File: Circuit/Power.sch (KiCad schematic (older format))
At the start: 23 parts

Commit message: Updated Lithium power circuit
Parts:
- removed C?: 470uF 16V, symbol CP
- removed C?: 47uF 16V, symbol C
- removed C?: C, symbol C
- removed D? (x4): SS14, symbol DIODE_SCHOTTKY
- removed L?: ?uH, symbol INDUCTOR_SMALL
- removed Q?: MOSFET_P, symbol MOSFET_P
- removed Q?: MOSFET_N, symbol MOSFET_N
- removed R? (x2): 100K, symbol R
- added C?: 220uF 16V, symbol CP
- added D? (x2): SS14, symbol DIODE_SCHOTTKY
- added L?: ???uH, symbol INDUCTOR
- added Q? (x2): SS9015, symbol TRANSISTOR_PNP
- added Q?: FDN340P, symbol MOSFET_P
- added R?: 100K, symbol R
- added R? (x2): 10K, symbol R
- Q201: renamed from Q?; value MOSFET_P -> FDN340P
- Q202: renamed from Q?; value AOD4189 -> FDN340P
- R204: renamed from R?; value ? -> 8.2K
- gave numbers to parts that had none: 8
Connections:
- net labels added: GBAT, GIN, VBAT
- net labels removed: VLOAD, ~CHARGER_ON
- wire segments 66 -> 58
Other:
- note added: ""Ideal Diode OR" circuit derived from "Type 3" shown at\nhttp://www.jiggerjuice.info/electronics/projects/power/ideal-diode.html\n\nSee attached LTSpice model file."
- note added: "Charging current\nIr = 220mA max"
- note added: "Solar input:\n7V open circuit voltage panel\nNominal 4-6V under load"
- note added: "USB Input:\nPreferred charging input if available, 4.5-5.5V"
- note removed: "AOD41897 gate\nthreshold = -1.7V - -3V"
- note removed: "Extra capacitance here\nensures VBAT P-FET switches\noff instantly, but slow to switch\non (allows VIN to switch off first)\n\nValue TBD"
- note removed: "~CHARGER_ON\nLOW = <1V\nHIGH = VOUT\n\n2N7002 gate\nthreshold = 1V - 2.5V"
- moved on the sheet: BAT201, D201, LED201, LED202, Q201, Q202, R201, R202, R203, R204, U201

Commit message: Updated to use esp12e
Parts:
- gave numbers to parts that had none: 10
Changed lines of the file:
@@
 LIBS:valves
 LIBS:ESPlant
+LIBS:ESP8266
 LIBS:ESPlant-cache
 EELAYER 25 0
@@
 $EndComp
 $Comp
-L GND #PWR202
+L GND #PWR18
 U 1 1 563C4E24
 P 4000 4650
-F 0 "#PWR202" H 4000 4400 50  0001 C CNN
+F 0 "#PWR18" H 4000 4400 50  0001 C CNN
 F 1 "GND" H 4000 4500 50  0000 C CNN
 F 2 "" H 4000 4650 60  0000 C CNN
@@
 $EndComp
 $Comp
-L GND #PWR201
+L GND #PWR17
 U 1 1 563C5B2C
 P 1150 1500
-F 0 "#PWR201" H 1150 1250 50  0001 C CNN
+F 0 "#PWR17" H 1150 1250 50  0001 C CNN
 F 1 "GND" H 1150 1350 50  0000 C CNN
 F 2 "" H 1150 1500 60  0000 C CNN
@@
 Connection ~ 5200 4500
 $Comp
-L DIODE_SCHOTTKY D?
+L DIODE_SCHOTTKY D3
 U 1 1 564177C3
 P 6850 1400
-F 0 "D?" H 6850 1500 40  0000 C CNN
+F 0 "D3" H 6850 1500 40  0000 C CNN
 F 1 "SS14" H 6850 1300 40  0000 C CNN
 F 2 "" H 6850 1400 60  0000 C CNN
@@
 $EndComp
 $Comp
-L TRANSISTOR_PNP Q?
+L TRANSISTOR_PNP Q2
 U 1 1 56417A02
 P 7250 3200
-F 0 "Q?" H 7250 3350 60  0000 R CNN
+F 0 "Q2" H 7250 3350 60  0000 R CNN
 F 1 "SS9015" H 7300 3000 60  0000 R CNN
 F 2 "" H 7250 3200 60  0000 C CNN
@@
 $EndComp
 $Comp
-L TRANSISTOR_PNP Q?
+L TRANSISTOR_PNP Q4
 U 1 1 56417AB5
 P 8950 3200
-F 0 "Q?" H 8950 3350 60  0000 R CNN
+F 0 "Q4" H 8950 3350 60  0000 R CNN
 F 1 "SS9015" H 9000 3000 60  0000 R CNN
 F 2 "" H 8950 3200 60  0000 C CNN
@@
 	7450 3200 8750 3200
 $Comp
-L R R?
+L R R7
 U 1 1 56417BF7
 P 8100 3900
-F 0 "R?" V 8180 3900 50  0000 C CNN
+F 0 "R7" V 8180 3900 50  0000 C CNN
 F 1 "100K" V 8100 3900 50  0000 C CNN
 F 2 "" V 8030 3900 30  0000 C CNN
@@
 $EndComp
 $Comp
-L R R?
+L R R6
 U 1 1 56417D21
 P 7150 3900
-F 0 "R?" V 7230 3900 50  0000 C CNN
+F 0 "R6" V 7230 3900 50  0000 C CNN
 F 1 "10K" V 7150 3900 50  0000 C CNN
 F 2 "" V 7080 3900 30  0000 C CNN
@@
 $EndComp
 $Comp
-L R R?
+L R R8
 U 1 1 56417E36
 P 9050 3900
-F 0 "R?" V 9130 3900 50  0000 C CNN
+F 0 "R8" V 9130 3900 50  0000 C CNN
 F 1 "10K" V 9050 3900 50  0000 C CNN
 F 2 "" V 8980 3900 30  0000 C CNN
@@
 	7150 3400 7150 3650
 $Comp
-L GND #PWR?
+L GND #PWR19
 U 1 1 56417FB3
 P 8100 4600
-F 0 "#PWR?" H 8100 4350 50  0001 C CNN
+F 0 "#PWR19" H 8100 4350 50  0001 C CNN
 F 1 "GND" H 8100 4450 50  0000 C CNN
 F 2 "" H 8100 4600 60  0000 C CNN
@@
 Connection ~ 7150 3550
 $Comp
-L MOSFET_P Q?
+L MOSFET_P Q3
 U 1 1 5641832A
 P 8400 2600
-F 0 "Q?" V 8200 2450 60  0000 R CNN
+F 0 "Q3" V 8200 2450 60  0000 R CNN
 F 1 "FDN340P" V 8300 2450 60  0000 R CNN
 F 2 "" H 8400 2600 60  0000 C CNN
@@
 $EndComp
 $Comp
-L DIODE_SCHOTTKY D?
+L DIODE_SCHOTTKY D4
 U 1 1 56418330
 P 8400 2100
-F 0 "D?" H 8400 2200 40  0000 C CNN
+F 0 "D4" H 8400 2200 40  0000 C CNN
 F 1 "SS14" H 8400 2000 40  0000 C CNN
 F 2 "" H 8400 2100 60  0000 C CNN
@@
 Connection ~ 7100 1800
 $Comp
-L INDUCTOR L?
+L INDUCTOR L1
 U 1 1 5641A74C
 P 9500 1800
-F 0 "L?" H 9400 1900 40  0000 C CNN
+F 0 "L1" H 9400 1900 40  0000 C CNN
 F 1 "???uH" H 9500 1750 40  0000 C CNN
 F 2 "" H 9500 1800 60  0000 C CNN
@@
 $EndComp
 $Comp
-L CP C?
+L CP C3
 U 1 1 5641A7A1
 P 10250 2150
-F 0 "C?" H 10275 2250 50  0000 L CNN
+F 0 "C3" H 10275 2250 50  0000 L CNN
 F 1 "220uF 16V" H 10275 2050 50  0000 L CNN
 F 2 "" H 10288 2000 30  0000 C CNN
@@
 	10250 2300 10250 2500
 $Comp
-L GND #PWR?
+L GND #PWR20
 U 1 1 5641AA9F
 P 10250 2500
-F 0 "#PWR?" H 10250 2250 50  0001 C CNN
+F 0 "#PWR20" H 10250 2250 50  0001 C CNN
 F 1 "GND" H 10250 2350 50  0000 C CNN
 F 2 "" H 10250 2500 60  0000 C CNN

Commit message: Change battery switching circuit to use MCP6002 comparator instead
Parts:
- removed C3: 220uF 16V, symbol CP
- removed D3, D4: SS14, symbol DIODE_SCHOTTKY
- removed L1: ???uH, symbol INDUCTOR
- removed Q2, Q4: SS9015, symbol TRANSISTOR_PNP
- removed R6, R8: 10K, symbol R
- removed R7: 100K, symbol R
- added C201: 100uF 16V, symbol C
- added C?: 100nF, symbol C
- added U202: MCP6002, symbol LM193
- renumbered Q3 to Q203
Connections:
- wire segments 58 -> 48
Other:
- note removed: ""Ideal Diode OR" circuit derived from "Type 3" shown at\nhttp://www.jiggerjuice.info/electronics/projects/power/ideal-diode.html\n\nSee attached LTSpice model file."

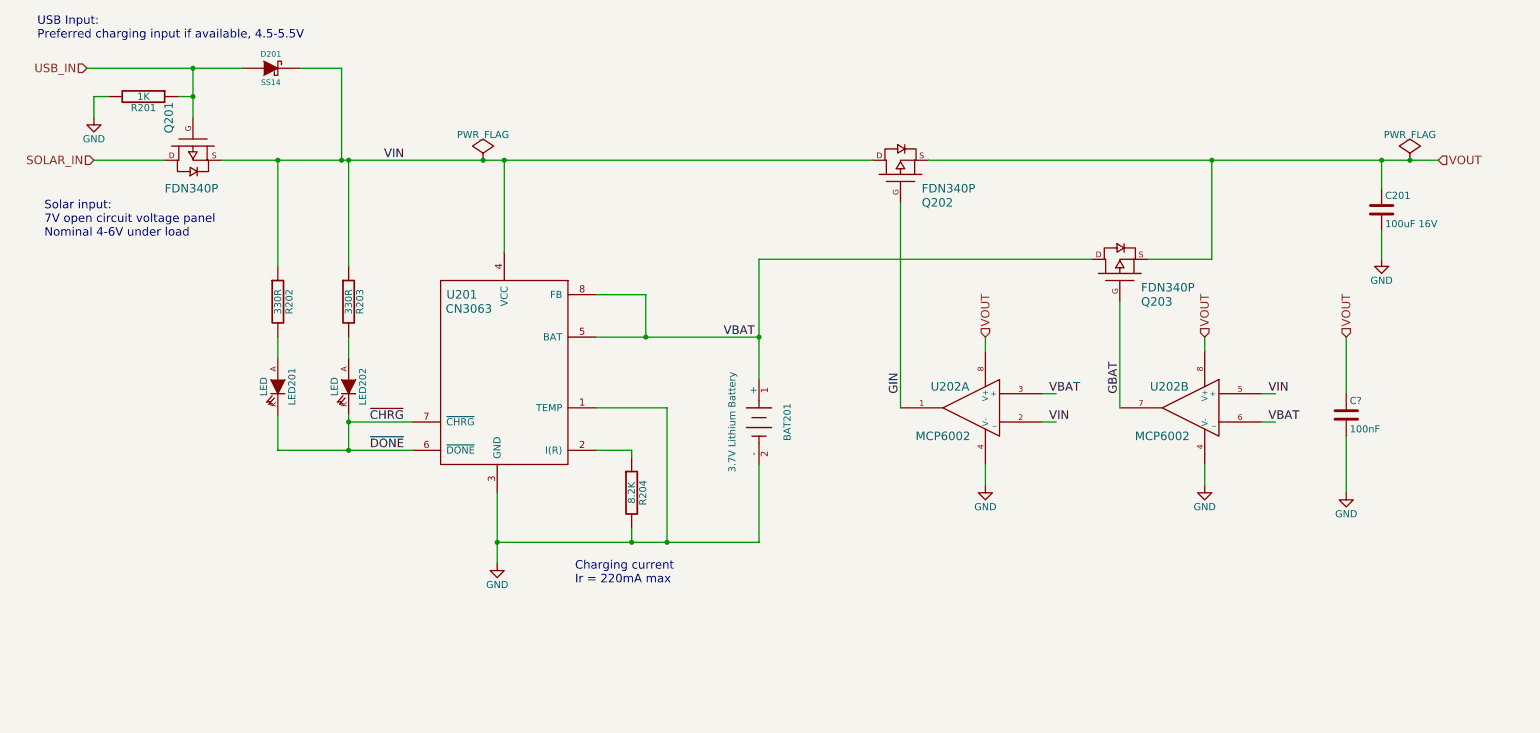
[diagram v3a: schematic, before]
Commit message: Add input cap to solar input
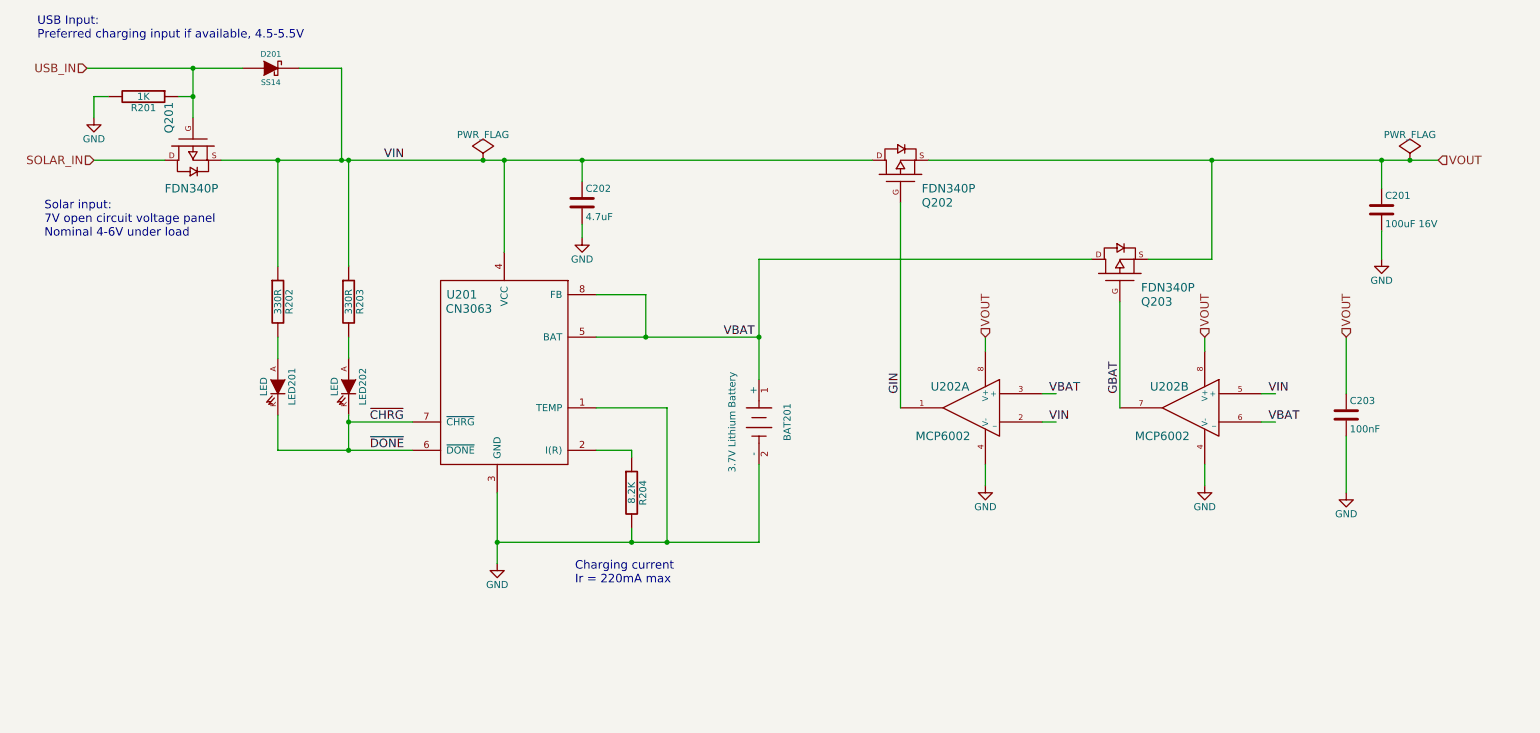
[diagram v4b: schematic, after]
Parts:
- added C202: 4.7uF, symbol C
- gave numbers to parts that had none: 1
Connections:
- wire segments 48 -> 68
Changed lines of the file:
@@
 LIBS:valves
 LIBS:ESPlant
+LIBS:ESP8266
 LIBS:ESPlant-cache
 EELAYER 25 0
@@
 $EndComp
 $Comp
-L GND #PWR018
+L GND #PWR202
 U 1 1 563C4E24
 P 4000 4650
-F 0 "#PWR018" H 4000 4400 50  0001 C CNN
+F 0 "#PWR202" H 4000 4400 50  0001 C CNN
 F 1 "GND" H 4000 4500 50  0000 C CNN
 F 2 "" H 4000 4650 60  0000 C CNN
@@
 $EndComp
 $Comp
-L GND #PWR019
+L GND #PWR201
 U 1 1 563C5B2C
 P 1150 1500
-F 0 "#PWR019" H 1150 1250 50  0001 C CNN
+F 0 "#PWR201" H 1150 1250 50  0001 C CNN
 F 1 "GND" H 1150 1350 50  0000 C CNN
 F 2 "" H 1150 1500 60  0000 C CNN
@@
 	5200 3550 5200 4500
 Wire Wire Line
-	4000 4150 4000 4650
+	4000 4150 4000 4500
+Wire Wire Line
+	4000 4500 4000 4650
 Wire Wire Line
 	4950 3900 4950 3850
@@
 	1150 1800 1650 1800
 Wire Wire Line
-	1850 1150 1850 1500
-Wire Wire Line
-	1100 1150 2200 1150
+	1850 1150 1850 1350
+Wire Wire Line
+	1850 1350 1850 1500
+Wire Wire Line
+	1100 1150 1850 1150
+Wire Wire Line
+	1850 1150 2200 1150
 Connection ~ 1850 1150
 Wire Wire Line
@@
 	1150 1350 1150 1500
 Wire Wire Line
-	2050 1800 6650 1800
+	2050 1800 2450 1800
+Wire Wire Line
+	2450 1800 2900 1800
+Wire Wire Line
+	2900 1800 2950 1800
+Wire Wire Line
+	2950 1800 3900 1800
+Wire Wire Line
+	3900 1800 4050 1800
+Wire Wire Line
+	4050 1800 4600 1800
+Wire Wire Line
+	4600 1800 6650 1800
 Wire Wire Line
 	2950 3650 3400 3650
@@
 Connection ~ 2950 1800
 Wire Wire Line
-	2950 3600 2950 3850
+	2950 3600 2950 3650
+Wire Wire Line
+	2950 3650 2950 3850
 Connection ~ 2950 3650
 Wire Wire Line
@@
 	6850 2100 6850 3550
 Wire Wire Line
-	2450 3850 3400 3850
+	2450 3850 2950 3850
+Wire Wire Line
+	2950 3850 3400 3850
 Wire Wire Line
 	2450 3050 2450 3200
@@
 Charging current\nIr = 220mA max
 Wire Wire Line
-	4000 4500 5850 4500
+	4000 4500 4950 4500
+Wire Wire Line
+	4950 4500 5200 4500
+Wire Wire Line
+	5200 4500 5850 4500
 Connection ~ 4000 4500
 Wire Wire Line
@@
 Connection ~ 5200 4500
 $Comp
-L GND #PWR020
+L GND #PWR204
 U 1 1 56417FB3
 P 7450 4100
-F 0 "#PWR020" H 7450 3850 50  0001 C CNN
+F 0 "#PWR204" H 7450 3850 50  0001 C CNN
 F 1 "GND" H 7450 3950 50  0000 C CNN
 F 2 "" H 7450 4100 60  0000 C CNN
@@
 $EndComp
 Wire Wire Line
-	4700 3050 5850 3050
+	4700 3050 5050 3050
+Wire Wire Line
+	5050 3050 5850 3050
 Connection ~ 5850 3050
 Wire Wire Line
-	5850 2500 5850 3350
+	5850 2500 5850 3050
+Wire Wire Line
+	5850 3050 5850 3350
 Wire Wire Line
 	5850 2500 8200 2500
@@
 GIN
 Wire Wire Line
-	7050 1800 10650 1800
+	7050 1800 9050 1800
+Wire Wire Line
+	9050 1800 10250 1800
+Wire Wire Line
+	10250 1800 10450 1800
+Wire Wire Line
+	10450 1800 10650 1800
 Wire Wire Line
 	10250 1800 10250 2000
@@
 	10250 2300 10250 2500
 $Comp
-L GND #PWR021
+L GND #PWR207
 U 1 1 5641AA9F
 P 10250 2500
-F 0 "#PWR021" H 10250 2250 50  0001 C CNN
+F 0 "#PWR207" H 10250 2250 50  0001 C CNN
 F 1 "GND" H 10250 2350 50  0000 C CNN
 F 2 "" H 10250 2500 60  0000 C CNN
@@
 VOUT
 $Comp
-L GND #PWR022
+L GND #PWR205
 U 1 1 5642C1C1
 P 9000 4100
-F 0 "#PWR022" H 9000 3850 50  0001 C CNN
+F 0 "#PWR205" H 9000 3850 50  0001 C CNN
 F 1 "GND" H 9000 3950 50  0000 C CNN
 F 2 "" H 9000 4100 60  0000 C CNN
@@
 	5850 4500 5850 3950
 $Comp
-L PWR_FLAG #FLG023
+L PWR_FLAG #FLG202
 U 1 1 5642D1CE
 P 10450 1800
-F 0 "#FLG023" H 10450 1895 50  0001 C CNN
+F 0 "#FLG202" H 10450 1895 50  0001 C CNN
 F 1 "PWR_FLAG" H 10450 1980 50  0000 C CNN
 F 2 "" H 10450 1800 60  0000 C CNN
@@
 Connection ~ 10450 1800
 $Comp
-L PWR_FLAG #FLG?
+L PWR_FLAG #FLG201
 U 1 1 5642D5A3
 P 3900 1800
-F 0 "#FLG?" H 3900 1895 50  0001 C CNN
+F 0 "#FLG201" H 3900 1895 50  0001 C CNN
 F 1 "PWR_FLAG" H 3900 1980 50  0000 C CNN
 F 2 "" H 3900 1800 60  0000 C CNN
@@
 Connection ~ 3900 1800
 $Comp
-L C C?
+L C C203
 U 1 1 5642D8F0
 P 10000 3600
-F 0 "C?" H 10025 3700 50  0000 L CNN
+F 0 "C203" H 10025 3700 50  0000 L CNN
 F 1 "100nF" H 10025 3500 50  0000 L CNN
 F 2 "" H 10038 3450 30  0000 C CNN
@@
 	10000 3750 10000 4150
 $Comp
-L GND #PWR?
+L GND #PWR206
 U 1 1 5642DA26
 P 10000 4150
-F 0 "#PWR?" H 10000 3900 50  0001 C CNN
+F 0 "#PWR206" H 10000 3900 50  0001 C CNN
 F 1 "GND" H 10000 4000 50  0000 C CNN
 F 2 "" H 10000 4150 60  0000 C CNN
@@
 Text HLabel 10000 3050 1    60   Input ~ 0
 VOUT
+$Comp
+L C C202
+U 1 1 5642CCB8
+P 4600 2100
+F 0 "C202" H 4625 2200 50  0000 L CNN
+F 1 "4.7uF" H 4625 2000 50  0000 L CNN
+F 2 "" H 4638 1950 30  0000 C CNN
+F 3 "" H 4600 2100 60  0000 C CNN
+	1    4600 2100
+	1    0    0    -1
+$EndComp
+Wire Wire Line
+	4600 1950 4600 1800
+Connection ~ 4600 1800
+Wire Wire Line
+	4600 2250 4600 2350
+$Comp
+L GND #PWR203
+U 1 1 5642CE9D
+P 4600 2350
+F 0 "#PWR203" H 4600 2100 50  0001 C CNN
+F 1 "GND" H 4600 2200 50  0000 C CNN
+F 2 "" H 4600 2350 60  0000 C CNN
+F 3 "" H 4600 2350 60  0000 C CNN
+	1    4600 2350
+	1    0    0    -1
+$EndComp
 $EndSCHEMATC

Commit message: Cleaned up main circuit diagram
Added some resistors where there weren't none...
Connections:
- wire segments 68 -> 50
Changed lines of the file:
@@
 	4700 3550 5200 3550
 Wire Wire Line
-	5200 3550 5200 4500
+	5200 4500 5200 3550
 Wire Wire Line
-	4000 4150 4000 4500
-Wire Wire Line
-	4000 4500 4000 4650
+	4000 4150 4000 4650
 Wire Wire Line
 	4950 3900 4950 3850
@@
 	1150 1800 1650 1800
 Wire Wire Line
-	1850 1150 1850 1350
+	1850 1150 1850 1500
 Wire Wire Line
-	1850 1350 1850 1500
-Wire Wire Line
-	1100 1150 1850 1150
-Wire Wire Line
-	1850 1150 2200 1150
+	1100 1150 2200 1150
 Connection ~ 1850 1150
 Wire Wire Line
 	2600 1150 2900 1150
 Wire Wire Line
-	2900 1150 2900 1800
+	2900 1800 2900 1150
 Connection ~ 2900 1800
 Wire Wire Line
@@
 	1150 1350 1150 1500
 Wire Wire Line
-	2050 1800 2450 1800
-Wire Wire Line
-	2450 1800 2900 1800
-Wire Wire Line
-	2900 1800 2950 1800
-Wire Wire Line
-	2950 1800 3900 1800
-Wire Wire Line
-	3900 1800 4050 1800
-Wire Wire Line
-	4050 1800 4600 1800
-Wire Wire Line
-	4600 1800 6650 1800
+	2050 1800 6650 1800
 Wire Wire Line
 	2950 3650 3400 3650
@@
 Connection ~ 2950 1800
 Wire Wire Line
-	2950 3600 2950 3650
-Wire Wire Line
-	2950 3650 2950 3850
+	2950 3600 2950 3850
 Connection ~ 2950 3650
 Wire Wire Line
@@
 	6850 2100 6850 3550
 Wire Wire Line
-	2450 3850 2950 3850
-Wire Wire Line
-	2950 3850 3400 3850
+	2450 3850 3400 3850
 Wire Wire Line
 	2450 3050 2450 3200
@@
 Charging current\nIr = 220mA max
 Wire Wire Line
-	4000 4500 4950 4500
-Wire Wire Line
-	4950 4500 5200 4500
-Wire Wire Line
-	5200 4500 5850 4500
+	4000 4500 5850 4500
 Connection ~ 4000 4500
 Wire Wire Line
@@
 $EndComp
 Wire Wire Line
-	4700 3050 5050 3050
-Wire Wire Line
-	5050 3050 5850 3050
+	4700 3050 5850 3050
 Connection ~ 5850 3050
 Wire Wire Line
-	5850 2500 5850 3050
-Wire Wire Line
-	5850 3050 5850 3350
+	5850 2500 5850 3350
 Wire Wire Line
 	5850 2500 8200 2500
@@
 GIN
 Wire Wire Line
-	7050 1800 9050 1800
-Wire Wire Line
-	9050 1800 10250 1800
-Wire Wire Line
-	10250 1800 10450 1800
-Wire Wire Line
-	10450 1800 10650 1800
+	7050 1800 10650 1800
 Wire Wire Line
 	10250 1800 10250 2000
